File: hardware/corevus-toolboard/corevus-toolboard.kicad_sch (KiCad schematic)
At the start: 85 parts, among them J1 MF3, J10 1x3P, J2 XH, J3 MF3, J4 XH, J5 XH, J6 XH, J7 XH, J8 pinheader, J9 XH, Q2 NMOS, Q3 AO3401A, Q4 AO3400, Q5 AO3400, SW3 RST, U1 LIS2DE12, U2 TPS54302, U3 STM32G431KBU3, U4 TMC2209-LA, U5 74LVC1G17, U6 SPX3819M5-L-3-3, Y1 XRCGB25

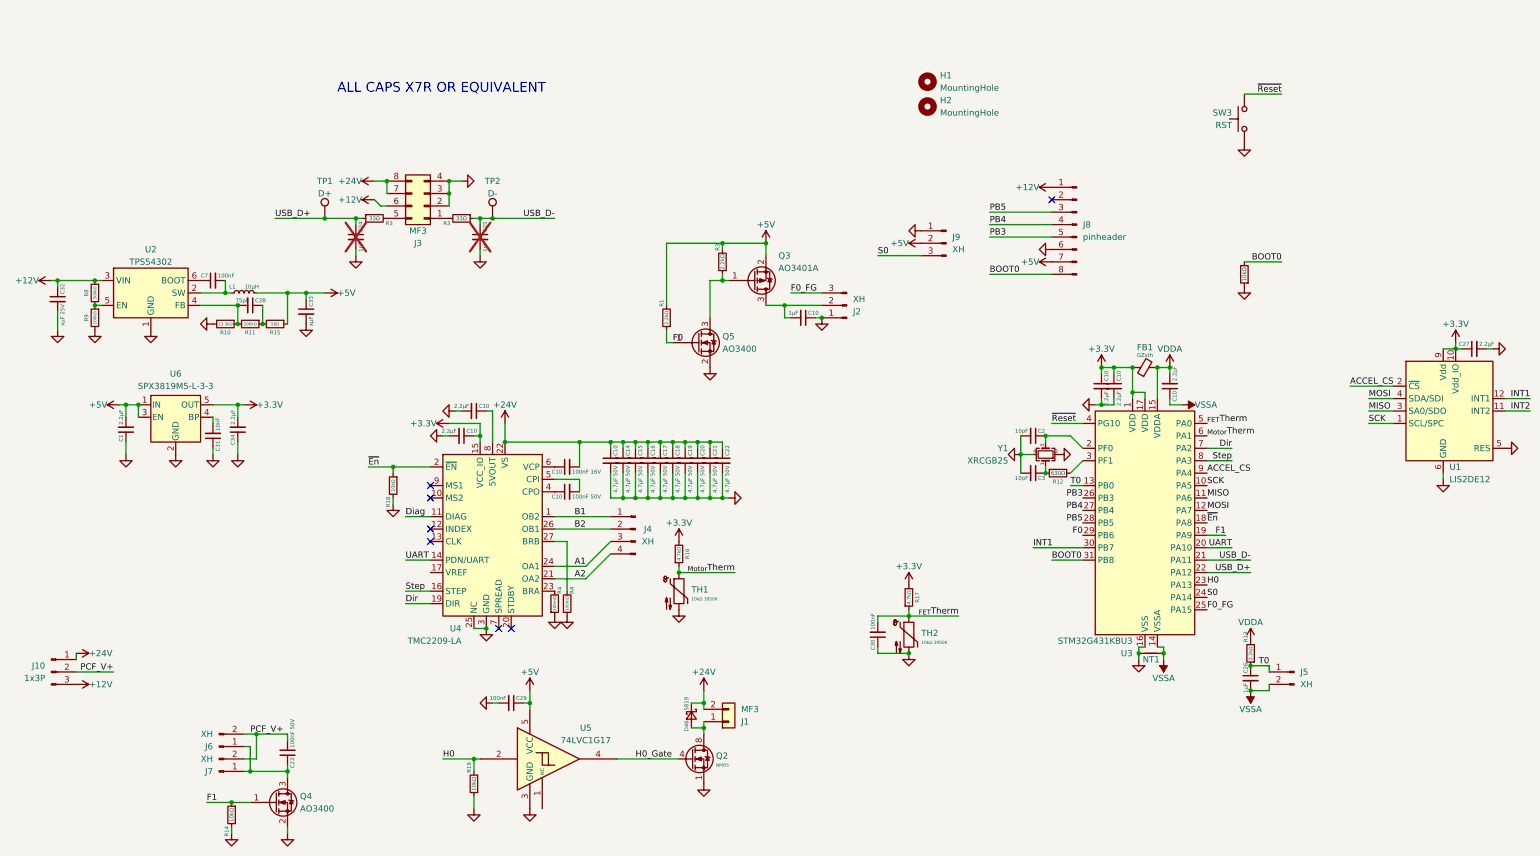
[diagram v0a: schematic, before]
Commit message: corevus toolboard v0.2 release (working), corevus-g v0.2 release (very much not working), m++ v0.1 (not working, needs a lot of bodges)
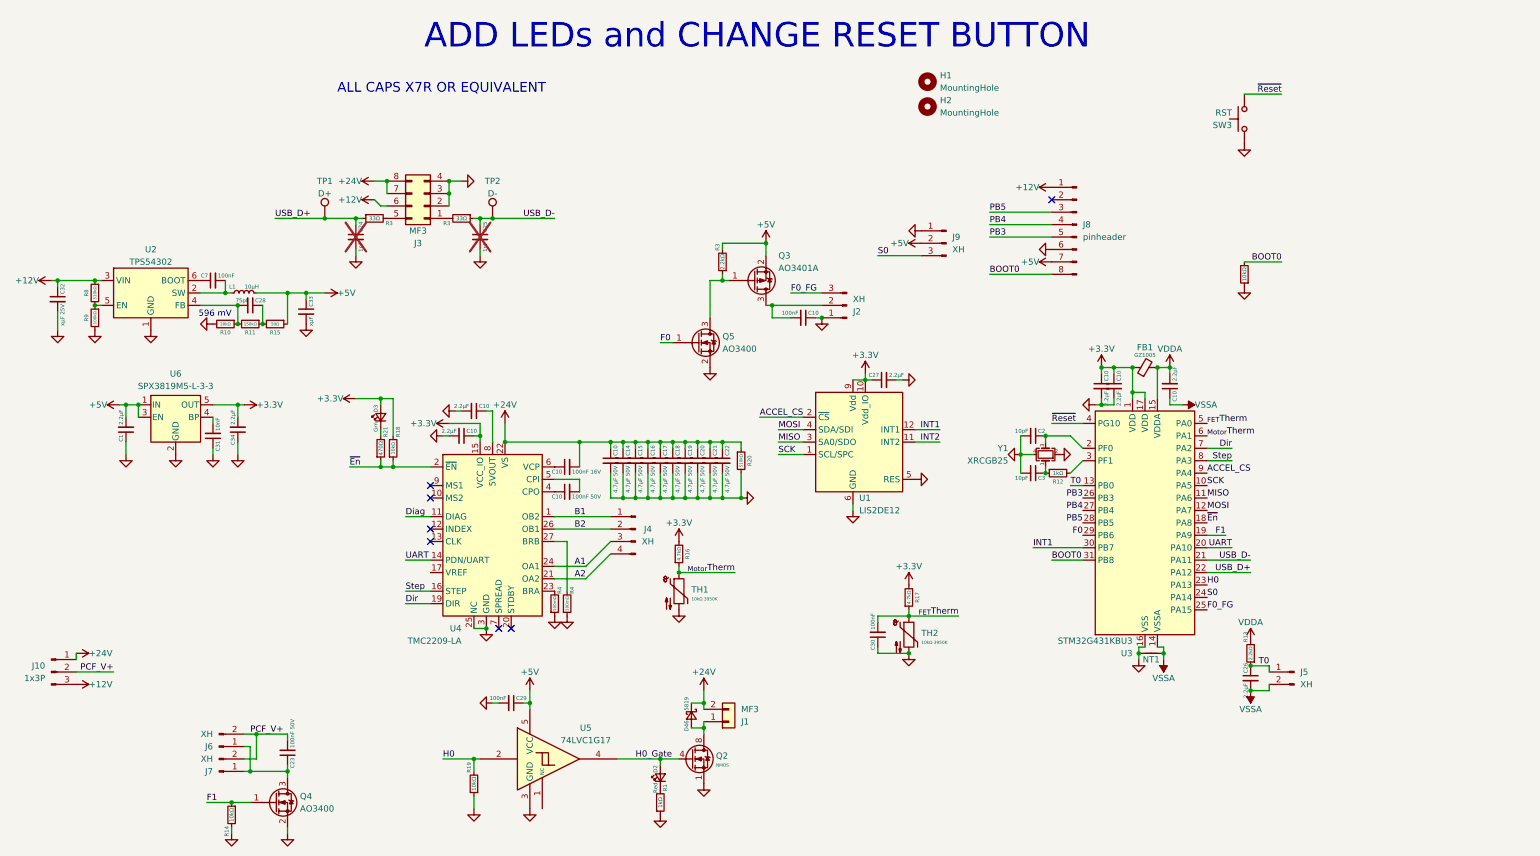
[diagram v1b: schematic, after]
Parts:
- added D2: Red, corevus:XL1606, symbol Device:LED_Small
- added D3: Grn, corevus:XL1606, symbol Device:LED_Small
- added R20: 510kΩ, AlphaLib:0402R, symbol Device:R_Small
- added R21: 470Ω, AlphaLib:0402R, symbol Device:R_Small
- C10: value 1μF -> 100nF
- C26: value 1µF -> 2.2µF
- FB1: value GZsth -> GZ1005
- R1: value 2.2kΩ -> 1kΩ
- R10: value 13.3kΩ -> 20kΩ
- R11: value 100kΩ -> 150kΩ
- R12: value 630Ω -> 1kΩ
- R8: value 500kΩ -> 510kΩ
- SW3: footprint corevus:ShouHan_TS3315A -> corevus:ShouHan_TS24CA
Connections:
- net +24V: now also R20.1
- net +3.3V: now also R18.2, D3.2 (A)
- net +5V: no longer R1.2
- net F0: no longer R1.1
- net GND: now also R1.1, SW3.2, R20.2; no longer R18.2, SW3.1
- net H0_Gate: now also D2.2 (A)
- net ~{En}: now also R21.1
- net ~{Reset}: now also SW3.1; no longer SW3.2
- new net: D2.1 (K), R1.2
- new net: D3.1 (K), R21.2
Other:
- note added: "596 mV"
- note added: "ADD LEDs and CHANGE RESET BUTTON"
- moved on the sheet: C27, R18, U1
